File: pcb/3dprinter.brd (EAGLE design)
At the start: 100 x 80 mm, 1 part

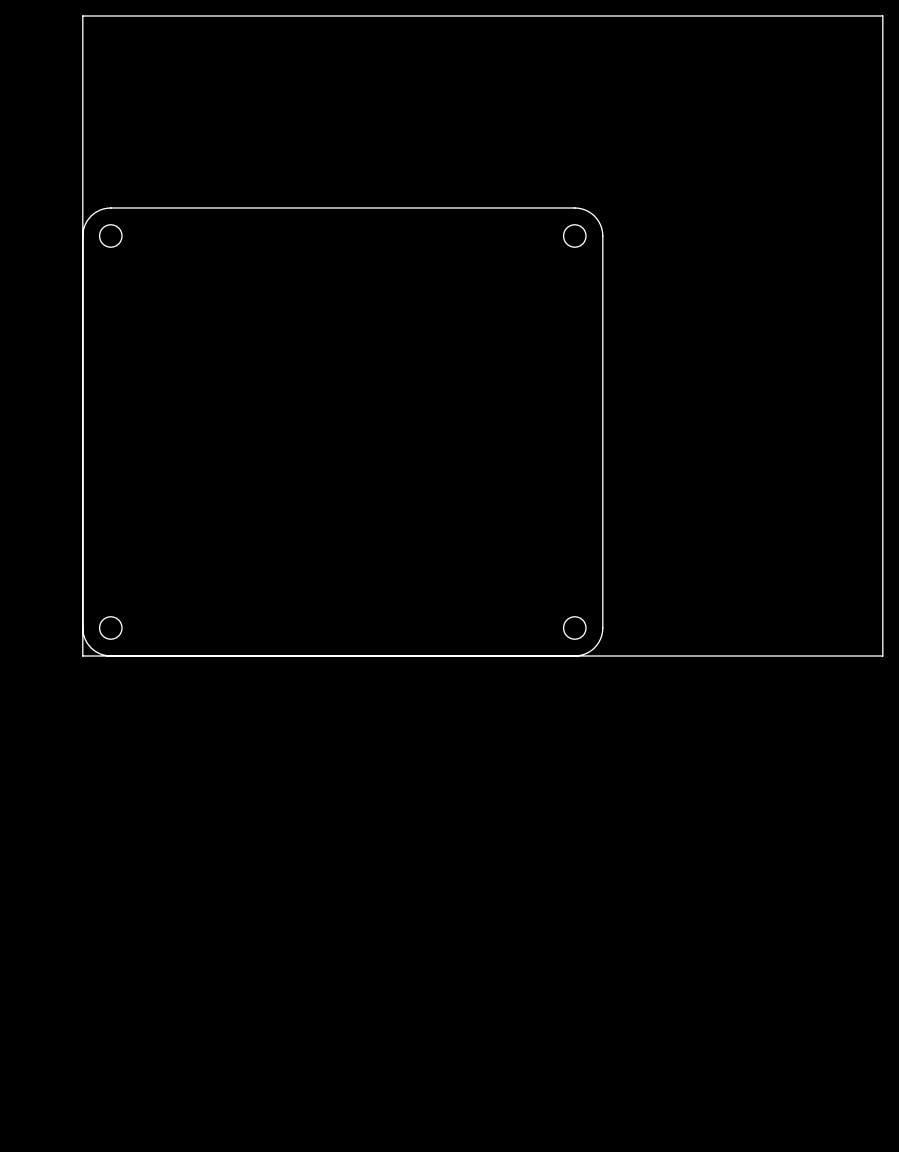
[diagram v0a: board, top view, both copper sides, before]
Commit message: Footprint of TMC2100 and reference schematic added
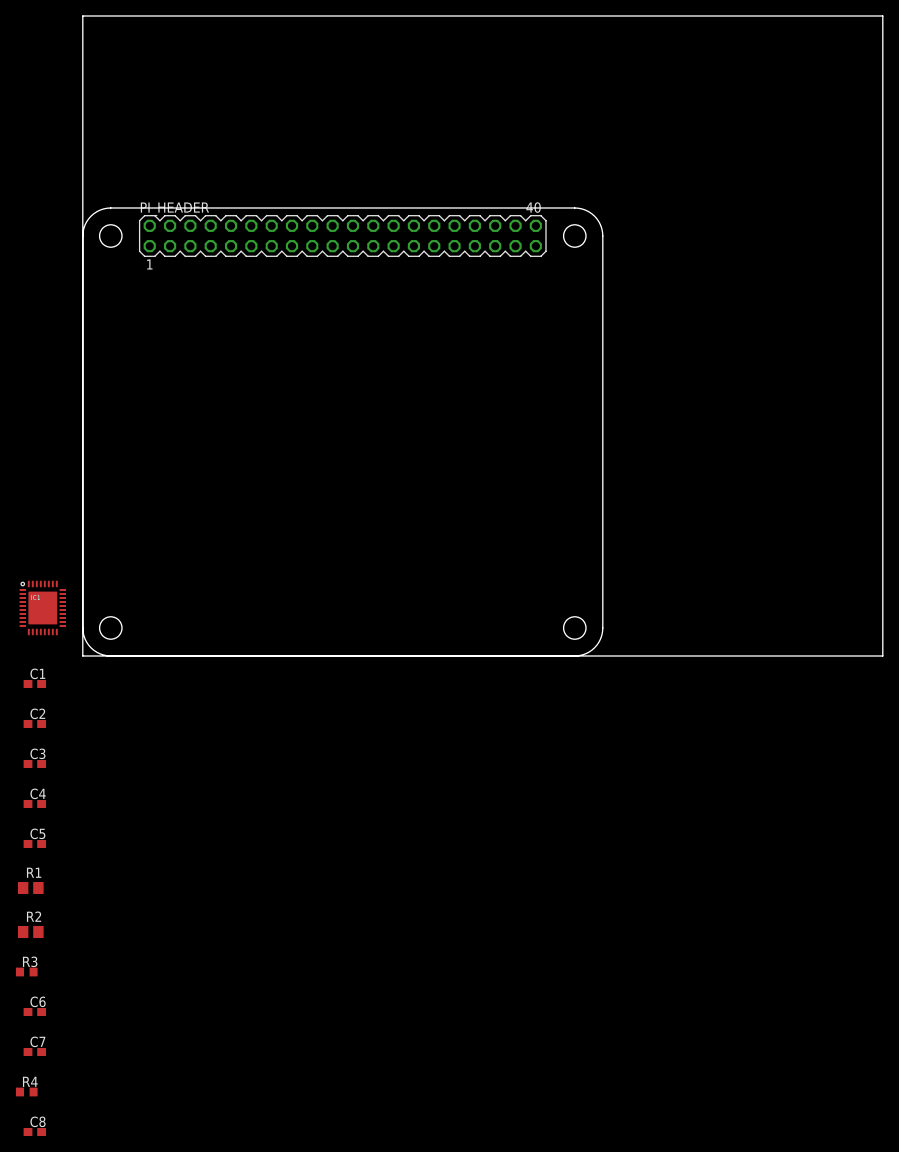
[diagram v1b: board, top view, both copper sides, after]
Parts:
- added C1, C2, C4, C5, C6: 100n, 3dprinter:C0603
- added C3: 1u, 3dprinter:C0603
- added C7: 470n, 3dprinter:C0603
- added C8: 4.7u, 3dprinter:C0603
- added IC1: TMC2100, 3dprinter:QFN36
- added PI_HEADER: (no value), 3dprinter:MA20-2
- added R1, R2: TBD, 3dprinter:R0805
- added R3: TBD, 3dprinter:R0603
- added R4: 2R2 / 3R3, 3dprinter:R0603
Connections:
- new net +12V: C1.2, C2.2, C3.2, C4.2, IC1.16, IC1.30, IC1.31
- new net +5V: C6.1, IC1.8
- new net 5V_M1: C8.1, IC1.25, R3.2, R4.2
- new net BRA_M1: IC1.33, R2.2
- new net BRB_M1: IC1.14, R1.2
- new net CFG1_M1: IC1.4
- new net CFG2_M1: IC1.3
- new net CPI_M1: C5.1, IC1.28
- new net CPO_M1: C5.2, IC1.27
- new net DIR_M1: IC1.7
- new net EN_M1: IC1.22
- new net GND: C1.1, C2.1, C3.1, C6.2, C7.2, C8.2, IC1.1, IC1.10, IC1.11, IC1.12, IC1.24, IC1.35, IC1.36, IC1.5, IC1.PAD, R1.1, R2.1
- new net IREF_M1: IC1.23, R3.1
- new net OA1_M1: IC1.34
- new net OA2_M1: IC1.32
- new net OB1_M1: IC1.13
- new net OB2_M1: IC1.15
- new net PI_3V31: PI_HEADER.1
- new net STEP_M1: IC1.6
- new net VCC_M1: C7.1, IC1.26, R4.1
- new net VCP_M1: C4.1, IC1.29
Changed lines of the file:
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@@
 <setting verticaltext="up"/>
 </settings>
-<grid distance="0.05" unitdist="inch" unit="inch" style="lines" multiple="1" display="no" altdistance="0.025" altunitdist="inch" altunit="inch"/>
+<grid distance="0.5" unitdist="mm" unit="mm" style="lines" multiple="1" display="yes" altdistance="0.1" altunitdist="mm" altunit="mm"/>
 <layers>
 <layer number="1" name="Top" color="4" fill="1" visible="yes" active="yes"/>
@@
 <elements>
 <element name="U$1" library="3dprinter" package="OUTLINE" value="OUTLINE" x="0" y="0"/>
+<element name="PI_HEADER" library="3dprinter" package="MA20-2" value="" x="32.5" y="52.5">
+<attribute name="MF" value="" x="32.5" y="52.5" size="1.778" layer="27" display="off"/>
+<attribute name="MPN" value="" x="32.5" y="52.5" size="1.778" layer="27" display="off"/>
+<attribute name="OC_FARNELL" value="unknown" x="32.5" y="52.5" size="1.778" layer="27" display="off"/>
+<attribute name="OC_NEWARK" value="unknown" x="32.5" y="52.5" size="1.778" layer="27" display="off"/>
+</element>
+<element name="IC1" library="3dprinter" package="QFN36" value="TMC2100" x="-5" y="6"/>
+<element name="C1" library="3dprinter" package="C0603" value="100n" x="-6" y="-3.5"/>
+<element name="C2" library="3dprinter" package="C0603" value="100n" x="-6" y="-8.5"/>
+<element name="C3" library="3dprinter" package="C0603" value="1u" x="-6" y="-13.5"/>
+<element name="C4" library="3dprinter" package="C0603" value="100n" x="-6" y="-18.5"/>
+<element name="C5" library="3dprinter" package="C0603" value="100n" x="-6" y="-23.5"/>
+<element name="R1" library="3dprinter" package="R0805" value="TBD" x="-6.5" y="-29"/>
+<element name="R2" library="3dprinter" package="R0805" value="TBD" x="-6.5" y="-34.5"/>
+<element name="R3" library="3dprinter" package="R0603" value="TBD" x="-7" y="-39.5"/>
+<element name="C6" library="3dprinter" package="C0603" value="100n" x="-6" y="-44.5"/>
+<element name="C7" library="3dprinter" package="C0603" value="470n" x="-6" y="-49.5"/>
+<element name="R4" library="3dprinter" package="R0603" value="2R2 / 3R3" x="-7" y="-54.5"/>
+<element name="C8" library="3dprinter" package="C0603" value="4.7u" x="-6" y="-59.5"/>
 </elements>
 <signals>
+<signal name="PI_3V31">
+<contactref element="PI_HEADER" pad="1"/>
+</signal>
+<signal name="PI_02_SDA1">
+</signal>
+<signal name="PI_03_SCL1">
+</signal>
+<signal name="PI_04">
+</signal>
+<signal name="PI_GND1">
+</signal>
+<signal name="PI_17">
+</signal>
+<signal name="PI_27">
+</signal>
+<signal name="PI_22">
+</signal>
+<signal name="PI_3V32">
+</signal>
+<signal name="PI_09_MISO">
+</signal>
+<signal name="PI_11_SCK">
+</signal>
+<signal name="PI_GND2">
+</signal>
+<signal name="PI_ID_SD">
+</signal>
+<signal name="PI_05">
+</signal>
+<signal name="PI_06">
+</signal>
+<signal name="PI_13">
+</signal>
+<signal name="PI_19">
+</signal>
+<signal name="PI_26">
+</signal>
+<signal name="PI_5V1">
+</signal>
+<signal name="PI_5V2">
+</signal>
+<signal name="PI_GND4">
+</signal>
+<signal name="PI_14_TXD0">
+</signal>
+<signal name="PI_15_RXD0">
+</signal>
+<signal name="PI_18">
+</signal>
+<signal name="PI_GND5">
+</signal>
+<signal name="PI_23">
+</signal>
+<signal name="PI_24">
+</signal>
+<signal name="PI_25">
+</signal>
+<signal name="PI_08_CE0">
+</signal>
+<signal name="PI_ID_SC">
+</signal>
+<signal name="PI_GND7">
+</signal>
+<signal name="PI_12">
+</signal>
+<signal name="PI_GND8">
+</signal>
+<signal name="PI_16">
+</signal>
+<signal name="PI_20">
+</signal>
+<signal name="+12V">
+<contactref element="IC1" pad="30"/>
+<contactref element="IC1" pad="16"/>
+<contactref element="IC1" pad="31"/>
+<contactref element="C2" pad="2"/>
+<contactref element="C3" pad="2"/>
+<contactref element="C1" pad="2"/>
+<contactref element="C4" pad="2"/>
+<wire x1="-5.15" y1="-13.5" x2="-5.15" y2="-18.5" width="0" layer="19" extent="1-1"/>
+<wire x1="-5.15" y1="-8.5" x2="-5.15" y2="-13.5" width="0" layer="19" extent="1-1"/>
+<wire x1="-5.15" y1="-3.5" x2="-5.15" y2="-8.5" width="0" layer="19" extent="1-1"/>
+<wire x1="-4.25" y1="3" x2="-5.15" y2="-3.5" width="0" layer="19" extent="1-1"/>
+<wire x1="-4.25" y1="9" x2="-4.25" y2="3" width="0" layer="19" extent="1-1"/>
+<wire x1="-3.75" y1="9" x2="-4.25" y2="9" width="0" layer="19" extent="1-1"/>
+</signal>
+<signal name="GND">
+<contactref element="C2" pad="1"/>
+<contactref element="C1" pad="1"/>
+<contactref element="C3" pad="1"/>
+<contactref element="R1" pad="1"/>
+<contactref element="R2" pad="1"/>
+<contactref element="IC1" pad="1"/>
+<contactref element="IC1" pad="11"/>
+<contactref element="IC1" pad="5"/>
+<contactref element="IC1" pad="36"/>
+<contactref element="IC1" pad="24"/>
+<contactref element="IC1" pad="10"/>
+<contactref element="IC1" pad="35"/>
+<contactref element="IC1" pad="12"/>
+<contactref element="IC1" pad="PAD"/>
+<contactref element="C6" pad="2"/>
+<contactref element="C7" pad="2"/>
+<contactref element="C8" pad="2"/>
+<wire x1="-5.15" y1="-49.5" x2="-5.15" y2="-59.5" width="0" layer="19" extent="1-1"/>
+<wire x1="-5.15" y1="-44.5" x2="-5.15" y2="-49.5" width="0" layer="19" extent="1-1"/>
+<wire x1="-7.45" y1="-34.5" x2="-5.15" y2="-44.5" width="0" layer="19" extent="1-1"/>
+<wire x1="-7.45" y1="-29" x2="-7.45" y2="-34.5" width="0" layer="19" extent="1-1"/>
+<wire x1="-6.85" y1="-13.5" x2="-7.45" y2="-29" width="0" layer="19" extent="1-1"/>
+<wire x1="-6.85" y1="-8.5" x2="-6.85" y2="-13.5" width="0" layer="19" extent="1-1"/>
+<wire x1="-6.85" y1="-3.5" x2="-6.85" y2="-8.5" width="0" layer="19" extent="1-1"/>
+<wire x1="-6.75" y1="3" x2="-6.85" y2="-3.5" width="0" layer="19" extent="1-1"/>
+<wire x1="-6.25" y1="3" x2="-6.75" y2="3" width="0" layer="19" extent="1-1"/>
+<wire x1="-7.5" y1="3.75" x2="-6.75" y2="3" width="0" layer="19" extent="1-1"/>
+<wire x1="-7.5" y1="6.25" x2="-7.5" y2="3.75" width="0" layer="19" extent="1-1"/>
+<wire x1="-7.5" y1="8.25" x2="-7.5" y2="6.25" width="0" layer="19" extent="1-1"/>
+<wire x1="-6.75" y1="9" x2="-7.5" y2="8.25" width="0" layer="19" extent="1-1"/>
+<wire x1="-6.25" y1="9" x2="-6.75" y2="9" width="0" layer="19" extent="1-1"/>
+<wire x1="-5" y1="6" x2="-7.5" y2="6.25" width="0" layer="19" extent="1-1"/>
+<wire x1="-2.5" y1="6.25" x2="-5" y2="6" width="0" layer="19" extent="1-1"/>
+</signal>
+<signal name="CPI_M1">
+<contactref element="IC1" pad="28"/>
+<contactref element="C5" pad="1"/>
+<wire x1="-2.5" y1="8.25" x2="-6.85" y2="-23.5" width="0" layer="19" extent="1-1"/>
+</signal>
+<signal name="CPO_M1">
+<contactref element="C5" pad="2"/>
+<contactref element="IC1" pad="27"/>
+<wire x1="-2.5" y1="7.75" x2="-5.15" y2="-23.5" width="0" layer="19" extent="1-1"/>
+</signal>
+<signal name="VCP_M1">
+<contactref element="IC1" pad="29"/>
+<contactref element="C4" pad="1"/>
+<wire x1="-3.25" y1="9" x2="-6.85" y2="-18.5" width="0" layer="19" extent="1-1"/>
+</signal>
+<signal name="OA1_M1">
+<contactref element="IC1" pad="34"/>
+</signal>
+<signal name="OA2_M1">
+<contactref element="IC1" pad="32"/>
+</signal>
+<signal name="OB1_M1">
+<contactref element="IC1" pad="13"/>
+</signal>
+<signal name="OB2_M1">
+<contactref element="IC1" pad="15"/>
+</signal>
+<signal name="BRB_M1">
+<contactref element="IC1" pad="14"/>
+<contactref element="R1" pad="2"/>
+<wire x1="-5.25" y1="3" x2="-5.55" y2="-29" width="0" layer="19" extent="1-1"/>
+</signal>
+<signal name="BRA_M1">
+<contactref element="IC1" pad="33"/>
+<contactref element="R2" pad="2"/>
+<wire x1="-5.25" y1="9" x2="-5.55" y2="-34.5" width="0" layer="19" extent="1-1"/>
+</signal>
+<signal name="5V_M1">
+<contactref element="R3" pad="2"/>
+<contactref element="R4" pad="2"/>
+<contactref element="IC1" pad="25"/>
+<contactref element="C8" pad="1"/>
+<wire x1="-6.15" y1="-54.5" x2="-6.85" y2="-59.5" width="0" layer="19" extent="1-1"/>
+<wire x1="-6.15" y1="-39.5" x2="-6.15" y2="-54.5" width="0" layer="19" extent="1-1"/>
+<wire x1="-2.5" y1="6.75" x2="-6.15" y2="-39.5" width="0" layer="19" extent="1-1"/>
+</signal>
+<signal name="IREF_M1">
+<contactref element="R3" pad="1"/>
+<contactref element="IC1" pad="23"/>
+<wire x1="-2.5" y1="5.75" x2="-7.85" y2="-39.5" width="0" layer="19" extent="1-1"/>
+</signal>
+<signal name="DIR_M1">
+<contactref element="IC1" pad="7"/>
+</signal>
+<signal name="STEP_M1">
+<contactref element="IC1" pad="6"/>
+</signal>
+<signal name="EN_M1">
+<contactref element="IC1" pad="22"/>
+</signal>
+<signal name="CFG1_M1">
+<contactref element="IC1" pad="4"/>
+</signal>
+<signal name="CFG2_M1">
+<contactref element="IC1" pad="3"/>
+</signal>
+<signal name="+5V">
+<contactref element="IC1" pad="8"/>
+<contactref element="C6" pad="1"/>
+<wire x1="-7.5" y1="4.75" x2="-6.85" y2="-44.5" width="0" layer="19" extent="1-1"/>
+</signal>
+<signal name="VCC_M1">
+<contactref element="C7" pad="1"/>
+<contactref element="IC1" pad="26"/>
+<contactref element="R4" pad="1"/>
+<wire x1="-6.85" y1="-49.5" x2="-7.85" y2="-54.5" width="0" layer="19" extent="1-1"/>
+<wire x1="-2.5" y1="7.25" x2="-6.85" y2="-49.5" width="0" layer="19" extent="1-1"/>
+</signal>
 </signals>
 </board>

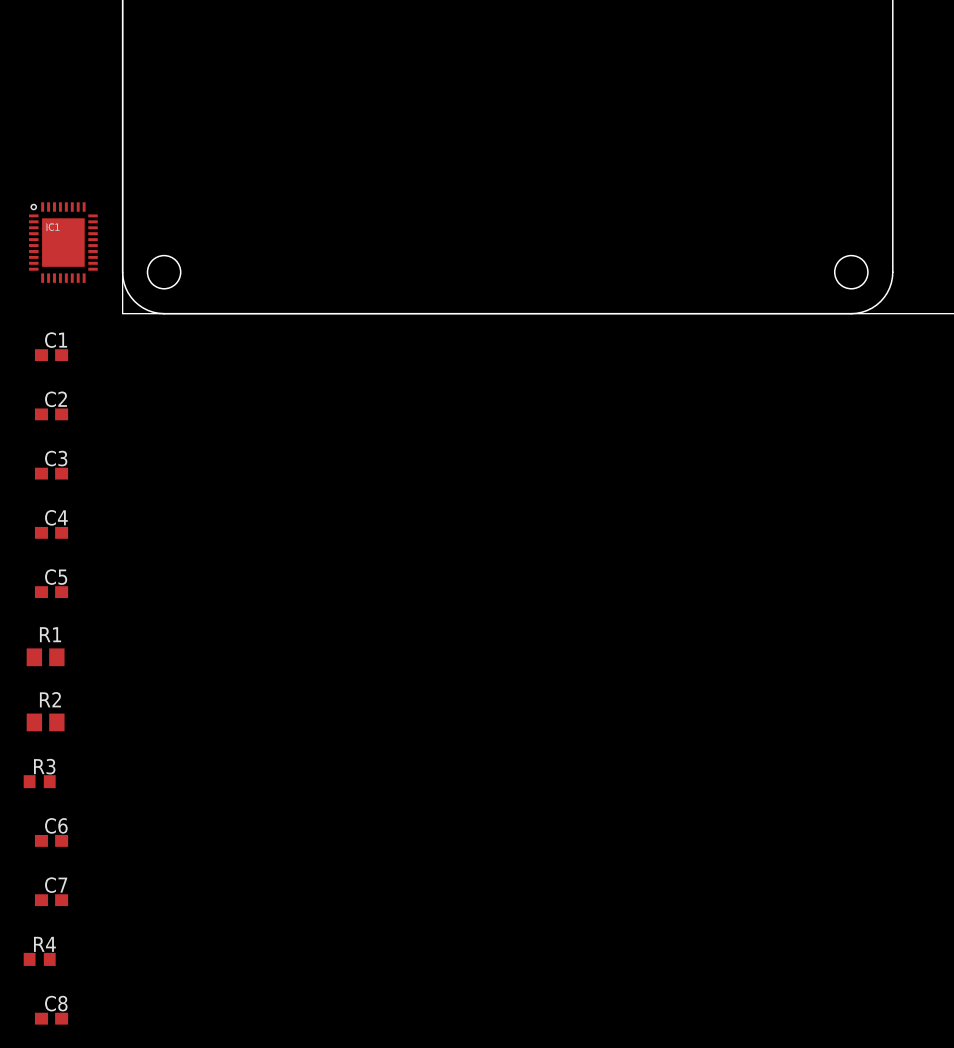
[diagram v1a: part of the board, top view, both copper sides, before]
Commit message: TMC2100 initial routing
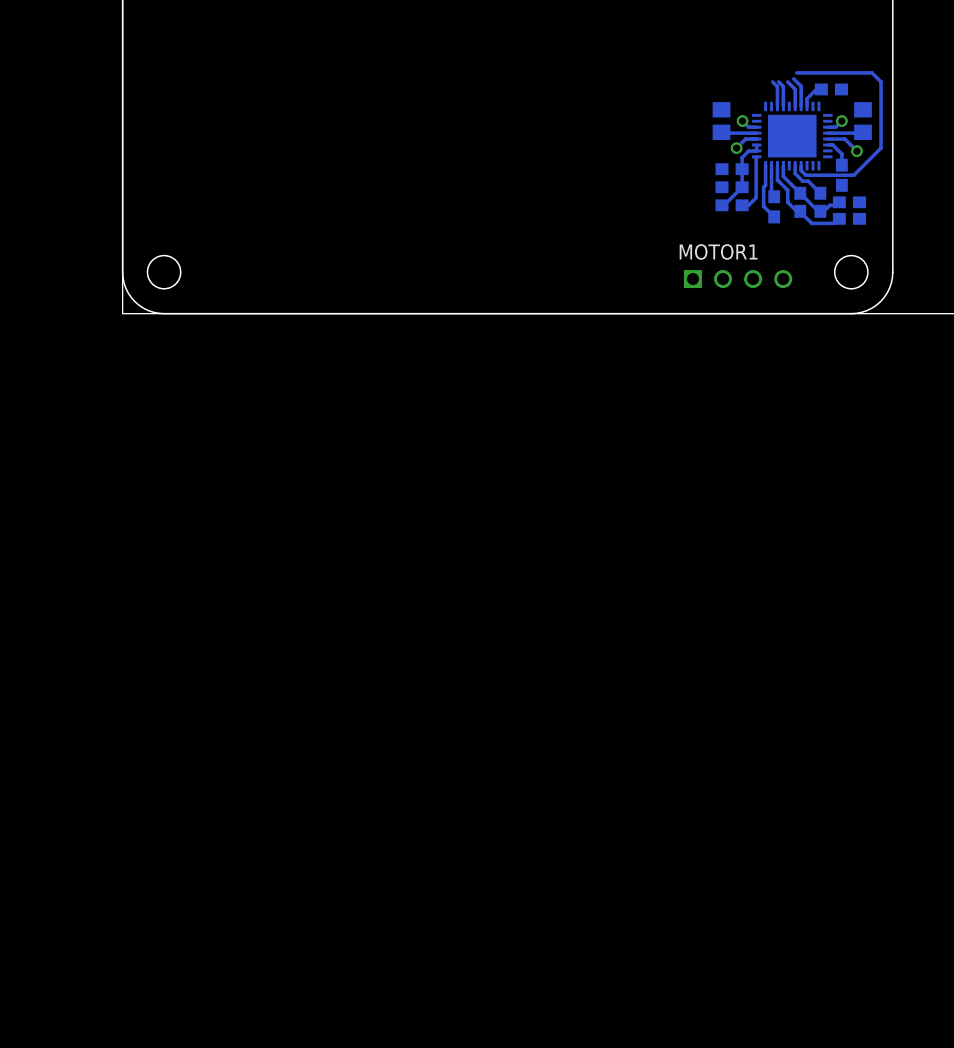
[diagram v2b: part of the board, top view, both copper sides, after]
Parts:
- added MOTOR1: (no value), 3dprinter:MA04-1
- moved C8 96.3 mm to (61.3, 9.40), flipped to the bottom, turned to 180 degrees
- moved C6 91.4 mm to (59.8, 18.9), flipped to the bottom, turned to 180 degrees
- moved R4 90.6 mm to (58.0, 8.64), flipped to the bottom, turned to 180 degrees
- moved C7 88.6 mm to (61.3, 8.00), flipped to the bottom, turned to 180 degrees
- moved R1 82.5 mm to (62.5, 16.3), flipped to the bottom, turned to 270 degrees
- moved R3 81.8 mm to (58.0, 10.2), flipped to the bottom
- moved R2 76.4 mm to (50.5, 16.3), flipped to the bottom, turned to 270 degrees
- moved C2 69.7 mm to (60.7, 11.7), flipped to the bottom, turned to 90 degrees
- moved C5 69.1 mm to (55.0, 9.02), flipped to the bottom, turned to 90 degrees
- moved C4 63.7 mm to (51.4, 9.14), flipped to the bottom
- moved C3 62.9 mm to (51.4, 12.2), flipped to the bottom, turned to 180 degrees
- moved IC1 62.2 mm to (56.5, 15.0), flipped to the bottom, turned to 270 degrees
- moved C1 59.2 mm to (51.4, 10.7), flipped to the bottom, turned to 180 degrees
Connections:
- net OA1_M1: now also MOTOR1.1
- net OA2_M1: now also MOTOR1.2
- net OB1_M1: now also MOTOR1.3
- net OB2_M1: now also MOTOR1.4
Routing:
- net EN_M1: track 0.00 -> 21.3 mm
- net +12V: track 0.00 -> 9.24 mm
- net VCC_M1: track 0.00 -> 8.72 mm
- net 5V_M1: track 0.00 -> 7.16 mm
- net VCP_M1: track 0.00 -> 4.92 mm
- net CPI_M1: track 0.00 -> 4.75 mm
- net IREF_M1: track 0.00 -> 3.48 mm
- net BRB_M1: track 0.00 -> 3.00 mm
- net BRA_M1: track 0.00 -> 3.00 mm
- net CPO_M1: track 0.00 -> 2.94 mm
- net OB2_M1: track 0.00 -> 2.88 mm, vias 0 -> 1
- net DIR_M1: track 0.00 -> 2.58 mm
- net OA2_M1: track 0.00 -> 2.44 mm, vias 0 -> 1
- net STEP_M1: track 0.00 -> 2.33 mm
- net CFG2_M1: track 0.00 -> 2.24 mm
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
